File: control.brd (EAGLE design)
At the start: 156 x 38 mm, 123 parts, among them IC3 ATTINY85-20S, U1 L293DD013TR

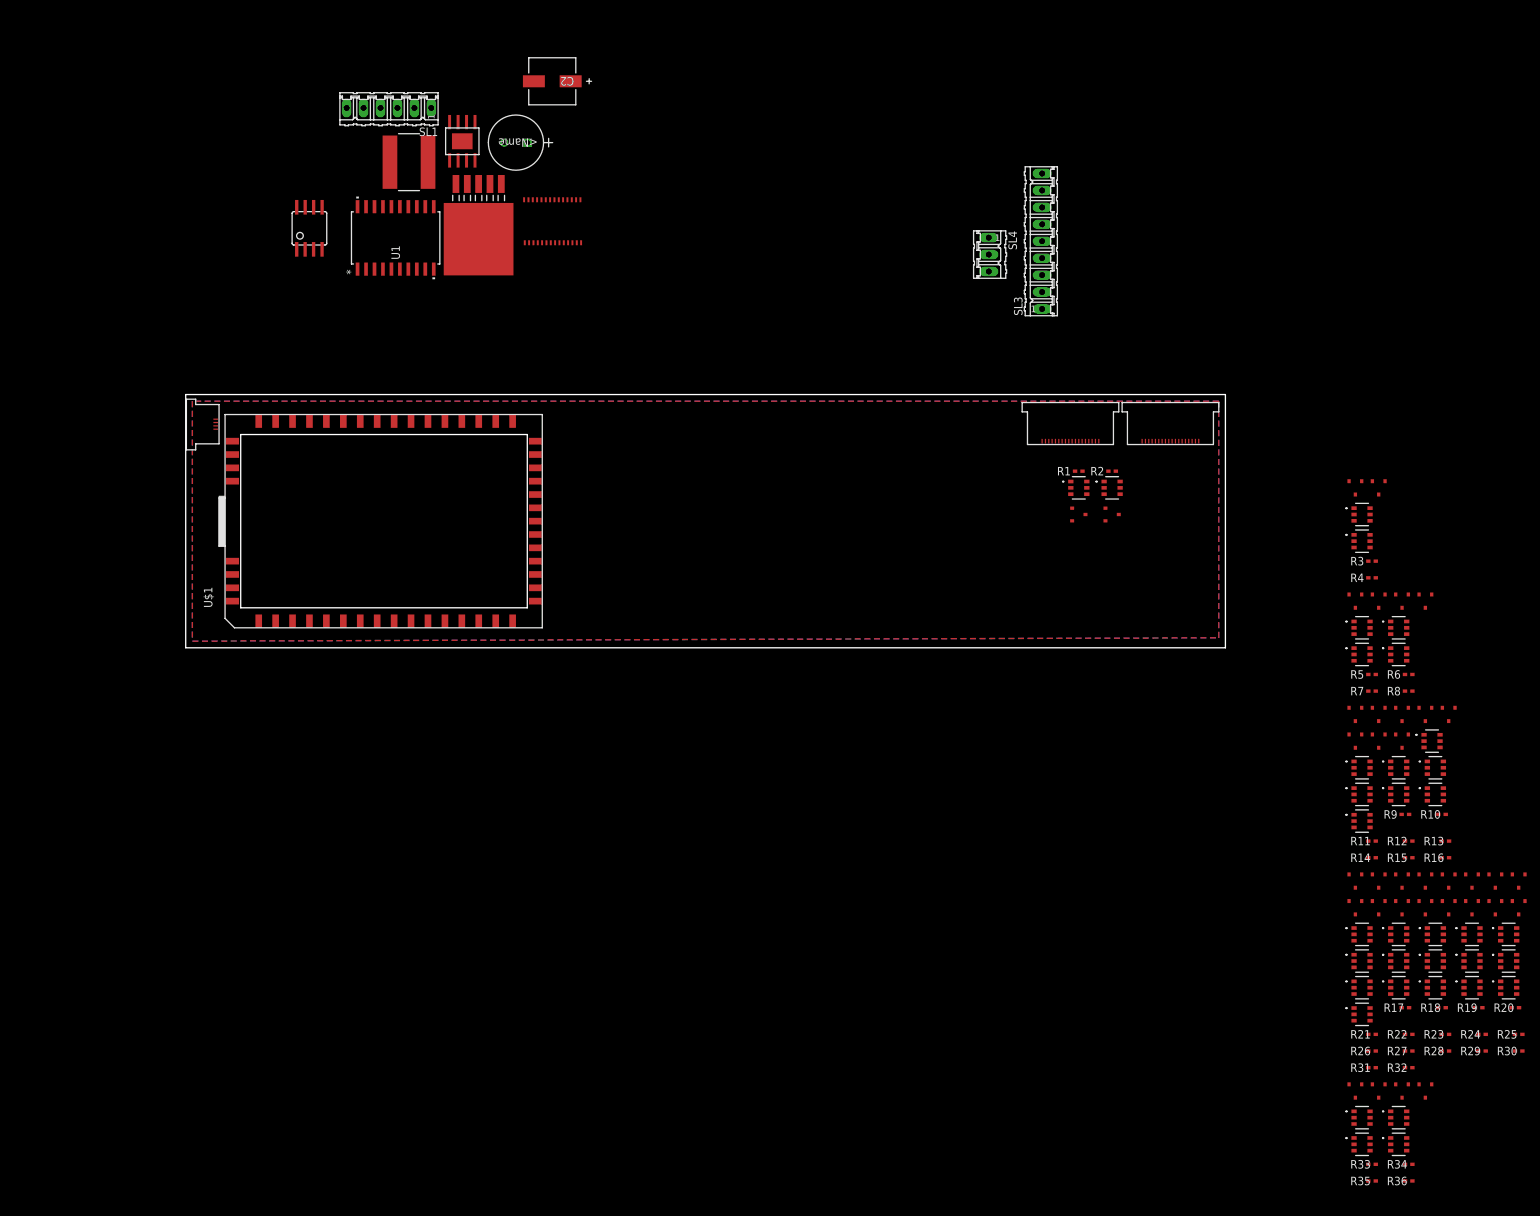
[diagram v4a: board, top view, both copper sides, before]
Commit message: removes excess led controllers
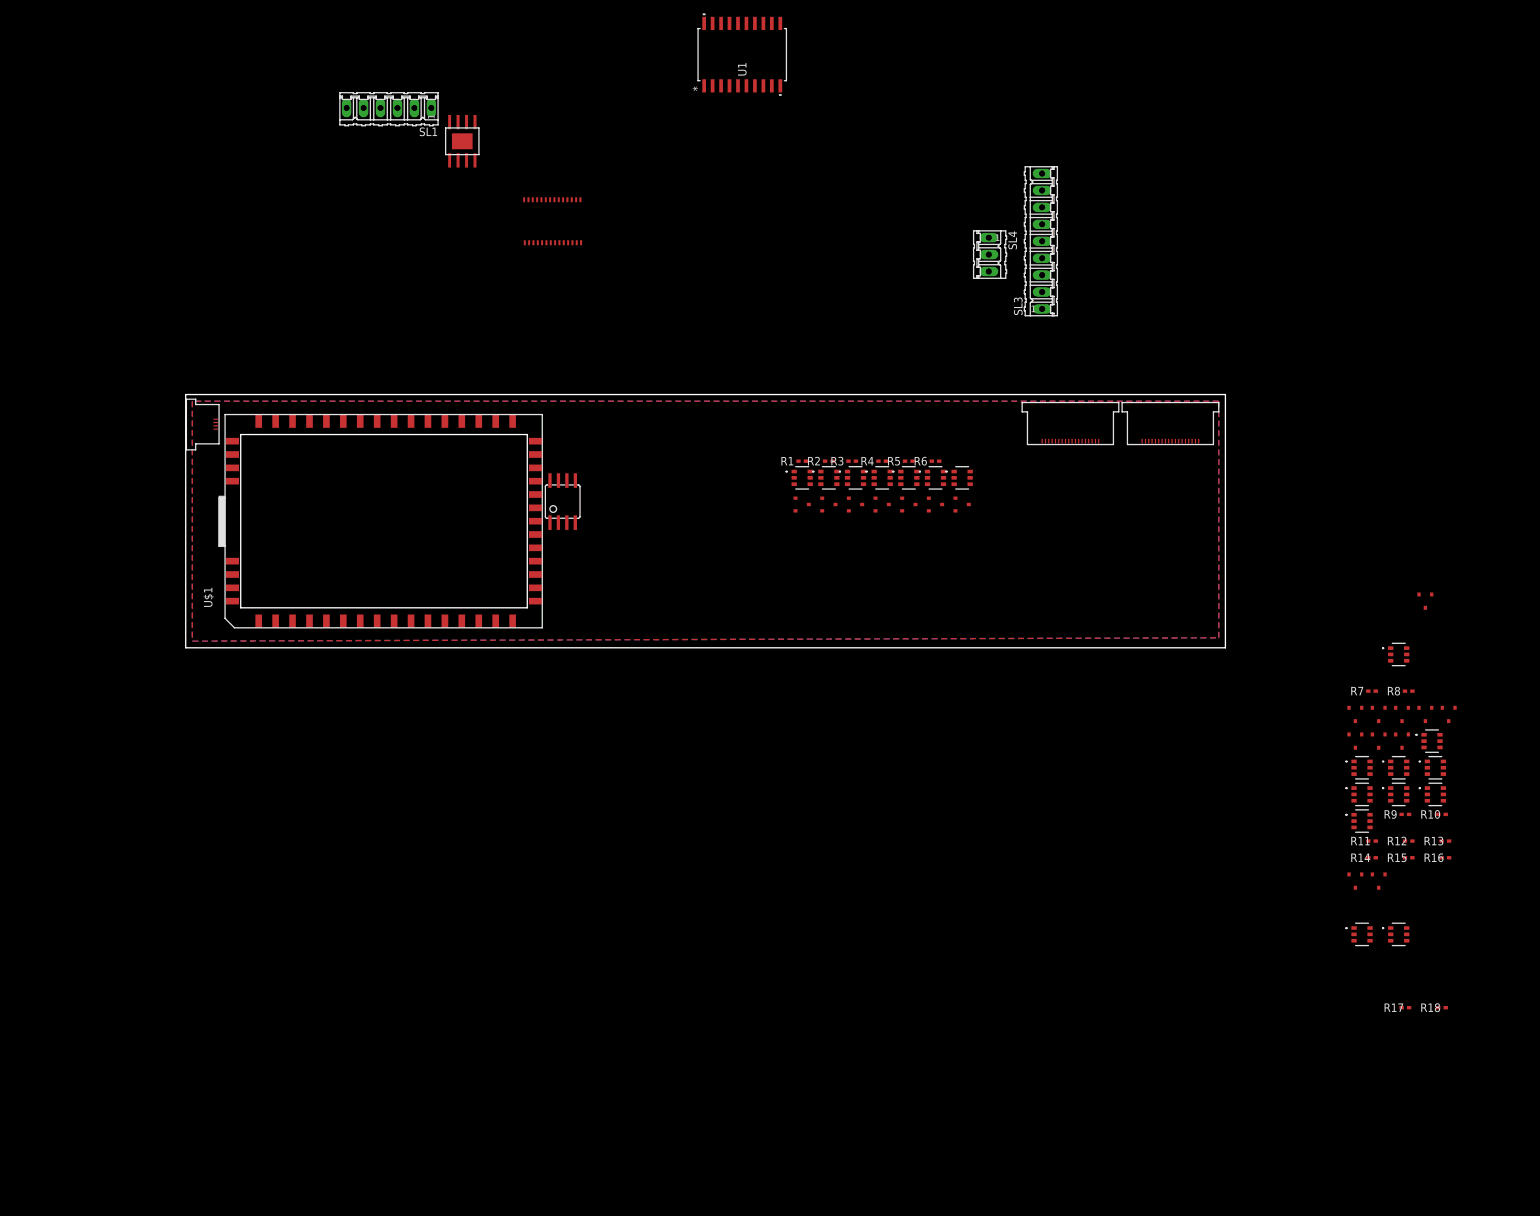
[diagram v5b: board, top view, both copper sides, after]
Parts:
- removed C1: UVR0J102MPD1TA, Smile_Shade:U1-M
- removed C2: UWX1C101MCL1GB, Smile_Shade:PCAP_6.3X5.4-ELECT
- removed R19, R20, R21, R22, R23, R24, R25, R26, R27, R28, R29, R30, R31, R32, R33, R34, R35, R36: RC0402JR-075R1L, Smile_Shade:RC0402N
- removed U$36: SRN8040-101M, Smile_Shade:IND_BOURNS_SRN8040
- removed U$41, U$46, U$48, U$50, U$52, U$54, U$56, U$58, U$60, U$62, U$64, U$66, U$68, U$70, U$72, U$74, U$76, U$78: 2N7002P, Smile_Shade:SOT23
- removed U$43: LM2576HVSX-5.0/NOPB, Smile_Shade:TS5B
- removed U$45, U$47, U$49, U$51, U$53, U$55, U$57, U$59, U$61, U$63, U$65, U$67, U$69, U$71, U$73, U$75, U$77, U$79: BCR420UW6-7, Smile_Shade:SOT26
- moved R3 79.4 mm to (100.0, 28.0)
- moved R6 77.9 mm to (112.5, 28.0)
- moved R5 76.5 mm to (108.5, 28.0)
- moved U$6 76.2 mm to (100.5, 25.5)
- moved R4 75.6 mm to (104.5, 28.0)
- moved U$5 75.0 mm to (100.5, 21.5), turned to 90 degrees
- moved U$7 74.5 mm to (104.5, 21.5), turned to 90 degrees
- moved U$12 73.1 mm to (112.5, 25.5)
- moved U$8 72.6 mm to (104.5, 25.5)
- moved U$10 71.6 mm to (108.5, 25.5)
- moved U$9 68.6 mm to (108.5, 21.5), turned to 90 degrees
- moved U$11 68.1 mm to (112.5, 21.5), turned to 90 degrees
- moved U$13 67.6 mm to (116.5, 21.5), turned to 90 degrees
- moved U$14 65.6 mm to (116.5, 25.5)
- moved U1 58.8 mm to (83.5, 89.0)
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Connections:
- removed net 48V: C2.1
- removed net GND18: R19.1, U$41.P$1, U$45.4
- removed net GND19: R20.1, U$46.P$1, U$47.4
- removed net GND20: R21.1, U$48.P$1, U$49.4
- removed net GND21: R22.1, U$50.P$1, U$51.4
- removed net GND22: R23.1, U$52.P$1, U$53.4
- removed net GND23: R24.1, U$54.P$1, U$55.4
- removed net GND24: R25.1, U$56.P$1, U$57.4
- removed net GND25: R26.1, U$58.P$1, U$59.4
- removed net GND26: R27.1, U$60.P$1, U$61.4
- removed net GND27: R28.1, U$62.P$1, U$63.4
- removed net GND28: R29.1, U$64.P$1, U$65.4
- removed net GND29: R30.1, U$66.P$1, U$67.4
- removed net GND30: R31.1, U$68.P$1, U$69.4
- removed net GND31: R32.1, U$70.P$1, U$71.4
- removed net GND32: R33.1, U$72.P$1, U$73.4
- removed net GND33: R34.1, U$74.P$1, U$75.4
- removed net GND34: R35.1, U$76.P$1, U$77.4
- removed net GND35: R36.1, U$78.P$1, U$79.4
- removed net LEDSTR_33: U$45.2, U$45.3, U$45.5
- removed net LEDSTR_34: U$47.2, U$47.3, U$47.5
- removed net LEDSTR_35: U$49.2, U$49.3, U$49.5
- removed net LEDSTR_36: U$51.2, U$51.3, U$51.5
- removed net LEDSTR_37: U$53.2, U$53.3, U$53.5
- removed net LEDSTR_38: U$55.2, U$55.3, U$55.5
- removed net LEDSTR_39: U$57.2, U$57.3, U$57.5
- removed net LEDSTR_40: U$59.2, U$59.3, U$59.5
- removed net LEDSTR_41: U$61.2, U$61.3, U$61.5
- removed net LEDSTR_42: U$63.2, U$63.3, U$63.5
- removed net LEDSTR_43: U$65.2, U$65.3, U$65.5
- removed net LEDSTR_44: U$67.2, U$67.3, U$67.5
- removed net LEDSTR_45: U$69.2, U$69.3, U$69.5
- removed net LEDSTR_46: U$71.2, U$71.3, U$71.5
- removed net LEDSTR_47: U$73.2, U$73.3, U$73.5
- removed net LEDSTR_48: U$75.2, U$75.3, U$75.5
- removed net LEDSTR_49: U$77.2, U$77.3, U$77.5
- removed net LEDSTR_50: U$79.2, U$79.3, U$79.5
- removed net N$33: U$36.1, U$43.2
- removed net N$34: C2.2, U$43.1
- removed net N$42: U$41.P$3, U$45.1
- removed net N$43: R19.2, U$45.6
- removed net N$44: U$46.P$3, U$47.1
- removed net N$45: R20.2, U$47.6
- removed net N$46: U$48.P$3, U$49.1
- removed net N$47: R21.2, U$49.6
- removed net N$48: U$50.P$3, U$51.1
- removed net N$49: R22.2, U$51.6
- removed net N$50: U$52.P$3, U$53.1
- removed net N$51: R23.2, U$53.6
- removed net N$52: U$54.P$3, U$55.1
- removed net N$53: R24.2, U$55.6
- removed net N$54: U$56.P$3, U$57.1
- removed net N$55: R25.2, U$57.6
- removed net N$56: U$58.P$3, U$59.1
- removed net N$57: R26.2, U$59.6
- removed net N$58: U$60.P$3, U$61.1
- removed net N$59: R27.2, U$61.6
- removed net N$60: U$62.P$3, U$63.1
- removed net N$61: R28.2, U$63.6
- removed net N$62: U$64.P$3, U$65.1
- removed net N$63: R29.2, U$65.6
- removed net N$64: U$66.P$3, U$67.1
- removed net N$65: R30.2, U$67.6
- removed net N$66: U$68.P$3, U$69.1
- removed net N$67: R31.2, U$69.6
- removed net N$68: U$70.P$3, U$71.1
- removed net N$69: R32.2, U$71.6
- removed net N$70: U$72.P$3, U$73.1
- removed net N$71: R33.2, U$73.6
- removed net N$72: U$74.P$3, U$75.1
- removed net N$73: R34.2, U$75.6
- removed net N$74: U$76.P$3, U$77.1
- removed net N$75: R35.2, U$77.6
- removed net N$76: U$78.P$3, U$79.1
- removed net N$77: R36.2, U$79.6
- removed net ZN33: U$41.P$2
- removed net ZN34: U$46.P$2
- removed net ZN35: U$48.P$2
- removed net ZN36: U$50.P$2
- removed net ZN37: U$52.P$2
- removed net ZN38: U$54.P$2
- removed net ZN39: U$56.P$2
- removed net ZN40: U$58.P$2
- removed net ZN41: U$60.P$2
- removed net ZN42: U$62.P$2
- removed net ZN43: U$64.P$2
- removed net ZN44: U$66.P$2
- removed net ZN45: U$68.P$2
- removed net ZN46: U$70.P$2
- removed net ZN47: U$72.P$2
- removed net ZN48: U$74.P$2
- removed net ZN49: U$76.P$2
- removed net ZN50: U$78.P$2
- net 5V: no longer C1.2, U$36.2, U$43.4
- net GND: no longer C1.1, U$43.3, U$43.5, U$43.6
